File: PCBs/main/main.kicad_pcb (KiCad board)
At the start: 2 copper layers, 91 x 56.5 mm, 6 parts, among them J1 chambers 03-04, J2 chambers 01-02, J3 chambers 05-06, J4 chambers 07-08, J5 chambers 9-10

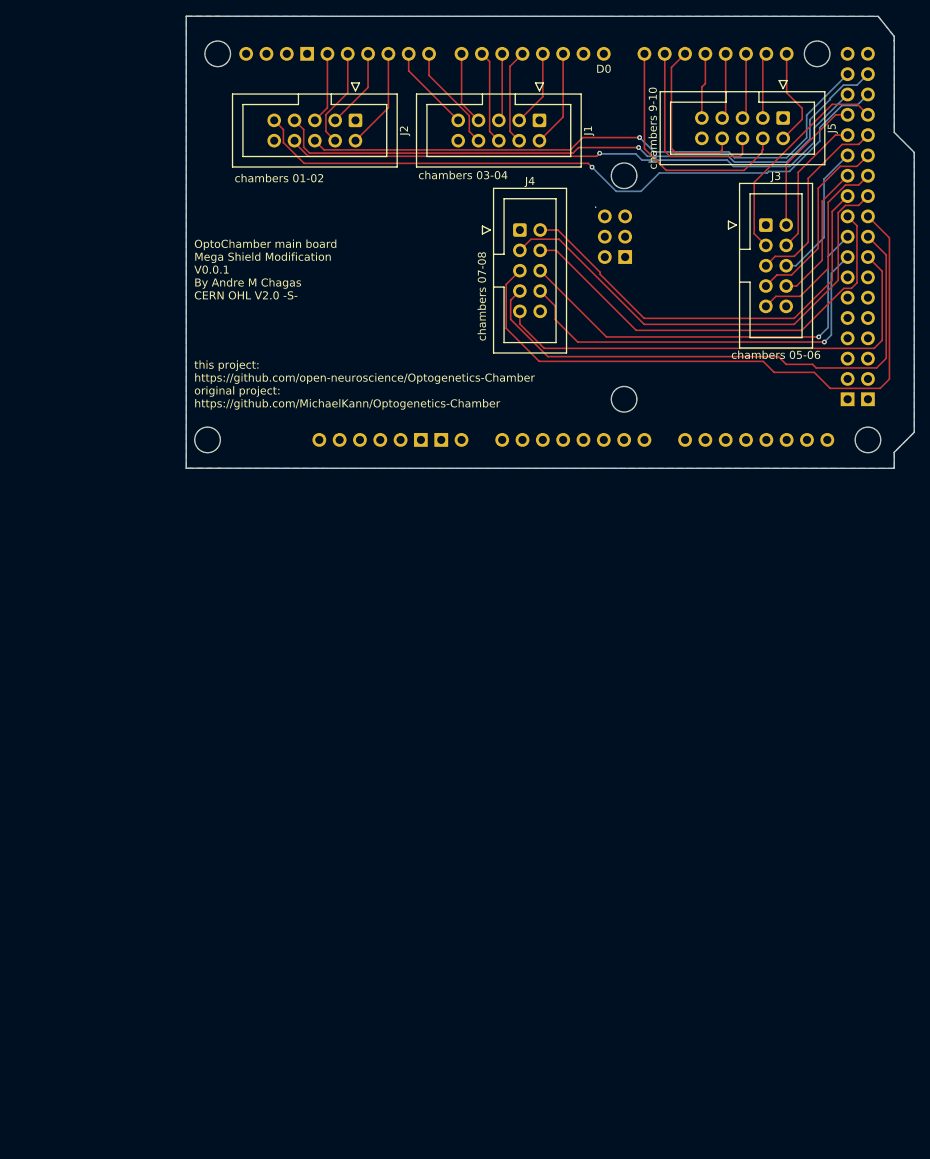
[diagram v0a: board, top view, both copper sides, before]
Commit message: create PCBs for easier replication of the system. It has been altered to use an arduino Mega, instead of an arduino Uno.
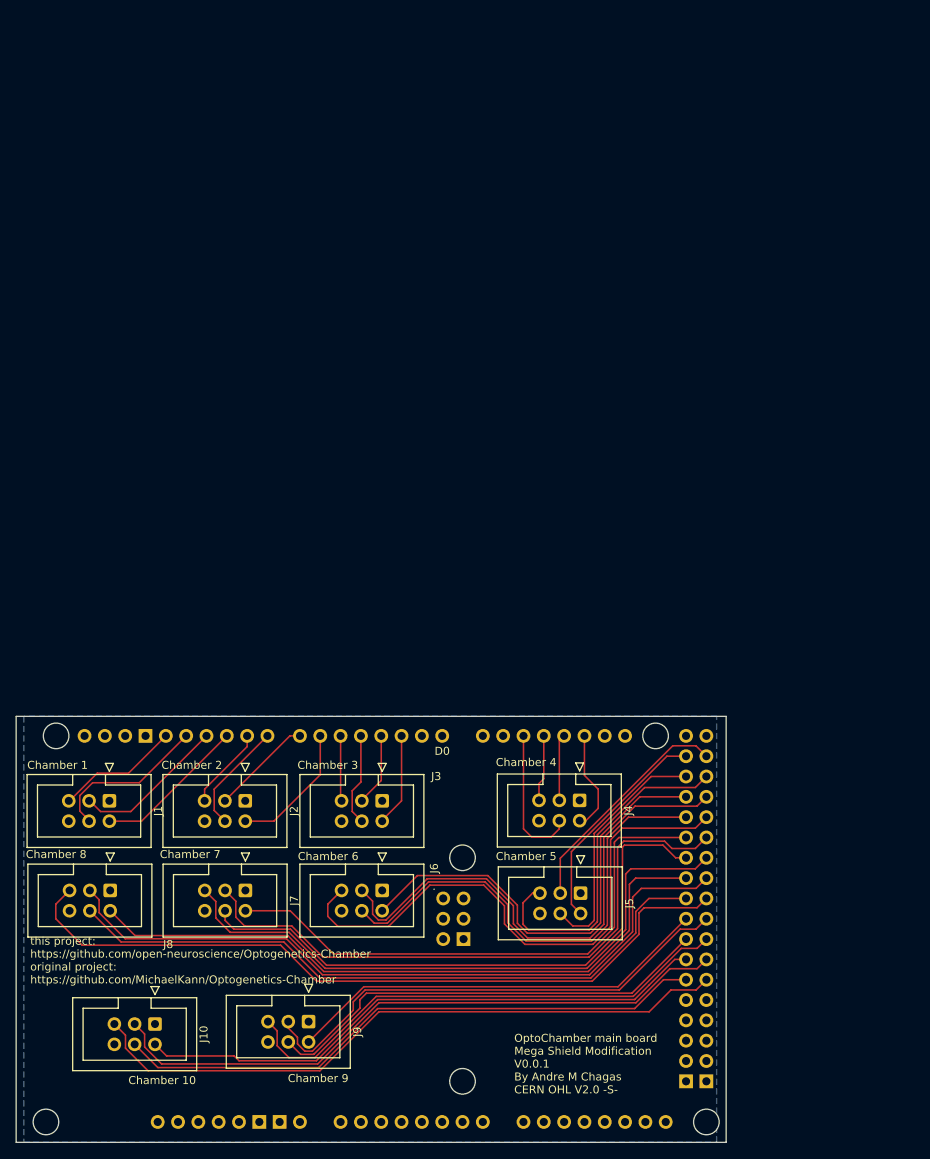
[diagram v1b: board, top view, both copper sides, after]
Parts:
- added J10: Chamber 10, Connector_IDC:IDC-Header_2x03_P2.54mm_Vertical, F.Cu at (94.6, 161.0)
- added J6: Chamber 6, Connector_IDC:IDC-Header_2x03_P2.54mm_Vertical, F.Cu at (123.0, 144.3)
- added J7: Chamber 7, Connector_IDC:IDC-Header_2x03_P2.54mm_Vertical, F.Cu at (105.9, 144.3)
- added J8: Chamber 8, Connector_IDC:IDC-Header_2x03_P2.54mm_Vertical, F.Cu at (89.0, 144.3)
- added J9: Chamber 9, Connector_IDC:IDC-Header_2x03_P2.54mm_Vertical, F.Cu at (113.8, 160.7)
- J1: value chambers 03-04 -> Chamber 1; footprint Connector_IDC:IDC-Header_2x05_P2.54mm_Vertical -> Connector_IDC:IDC-Header_2x03_P2.54mm_Vertical
- J2: value chambers 01-02 -> Chamber 2; footprint Connector_IDC:IDC-Header_2x05_P2.54mm_Vertical -> Connector_IDC:IDC-Header_2x03_P2.54mm_Vertical
- J3: value chambers 05-06 -> Chamber 3; footprint Connector_IDC:IDC-Header_2x05_P2.54mm_Vertical -> Connector_IDC:IDC-Header_2x03_P2.54mm_Vertical
- J4: value chambers 07-08 -> Chamber 4; footprint Connector_IDC:IDC-Header_2x05_P2.54mm_Vertical -> Connector_IDC:IDC-Header_2x03_P2.54mm_Vertical
- J5: value chambers 9-10 -> Chamber 5; footprint Connector_IDC:IDC-Header_2x05_P2.54mm_Vertical -> Connector_IDC:IDC-Header_2x03_P2.54mm_Vertical
- moved J1 100.6 mm to (88.9, 133.1)
- moved J5 100.1 mm to (147.8, 144.6)
- moved A2 87.6 mm to (67.0, 175.7)
- moved J3 86.5 mm to (123.0, 133.1), turned to -90 degrees
- moved J2 86.2 mm to (105.9, 133.1)
- moved J4 71.7 mm to (147.7, 133.0), turned to -90 degrees
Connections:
- A2 pad D10: Net-(J2-Pin_2) -> Net-(J1-Pin_2)
- A2 pad D11: Net-(J2-Pin_3) -> Net-(J1-Pin_3)
- A2 pad D12: Net-(J2-Pin_4) -> Net-(J1-Pin_4)
- A2 pad D13: Net-(J2-Pin_5) -> Net-(J1-Pin_5)
- A2 pad D14: Net-(A2-D14/TX3) -> unconnected-(A2-D14/TX3-PadD14)
- A2 pad D15: Net-(A2-D15/RX3) -> unconnected-(A2-D15/RX3-PadD15)
- A2 pad D20: Net-(A2-D20/SDA) -> unconnected-(A2-D20/SDA-PadD20)
- A2 pad D21: Net-(A2-D21/SCL) -> unconnected-(A2-D21/SCL-PadD21)
- A2 pad D22: Net-(J2-Pin_6) -> Net-(J5-Pin_2)
- A2 pad D23: Net-(J2-Pin_7) -> Net-(J5-Pin_3)
- A2 pad D24: Net-(J2-Pin_8) -> Net-(J5-Pin_4)
- A2 pad D25: Net-(J2-Pin_9) -> Net-(J5-Pin_5)
- A2 pad D26: Net-(J3-Pin_2) -> Net-(J6-Pin_2)
- A2 pad D27: Net-(J3-Pin_3) -> Net-(J6-Pin_3)
- A2 pad D28: Net-(J3-Pin_4) -> Net-(J6-Pin_4)
- A2 pad D29: Net-(J3-Pin_5) -> Net-(J6-Pin_5)
- A2 pad D30: Net-(J3-Pin_6) -> Net-(J7-Pin_2)
- A2 pad D31: Net-(J3-Pin_7) -> Net-(J7-Pin_3)
- A2 pad D32: Net-(J3-Pin_8) -> Net-(J7-Pin_4)
- A2 pad D33: Net-(J3-Pin_9) -> Net-(J7-Pin_5)
- A2 pad D34: Net-(J4-Pin_2) -> Net-(J8-Pin_2)
- A2 pad D35: Net-(J4-Pin_3) -> Net-(J8-Pin_3)
- A2 pad D36: Net-(J4-Pin_4) -> Net-(J8-Pin_4)
- A2 pad D37: Net-(J4-Pin_5) -> Net-(J8-Pin_5)
- A2 pad D38: Net-(J4-Pin_6) -> Net-(J9-Pin_2)
- A2 pad D39: Net-(J4-Pin_7) -> Net-(J9-Pin_3)
- A2 pad D4: Net-(J1-Pin_4) -> Net-(J3-Pin_4)
- A2 pad D40: Net-(J4-Pin_8) -> Net-(J9-Pin_4)
- A2 pad D41: Net-(J4-Pin_9) -> Net-(J9-Pin_5)
- A2 pad D42: unconnected-(A2-PadD42) -> Net-(J10-Pin_2)
- A2 pad D43: unconnected-(A2-PadD43) -> Net-(J10-Pin_3)
- A2 pad D44: unconnected-(A2-PadD44) -> Net-(J10-Pin_4)
- A2 pad D45: unconnected-(A2-PadD45) -> Net-(J10-Pin_5)
- A2 pad D5: Net-(J1-Pin_5) -> Net-(J3-Pin_5)
- A2 pad D6: Net-(J1-Pin_6) -> Net-(J2-Pin_2)
- A2 pad D7: Net-(J1-Pin_7) -> Net-(J2-Pin_3)
- A2 pad D8: Net-(J1-Pin_8) -> Net-(J2-Pin_4)
- A2 pad D9: Net-(J1-Pin_9) -> Net-(J2-Pin_5)
- J1 pad 2: Net-(A2-D2_INT0) -> Net-(J1-Pin_2)
- J1 pad 3: Net-(A2-D3_INT1) -> Net-(J1-Pin_3)
- J1 pad 6: Net-(J1-Pin_6) -> unconnected-(J1-Pin_6-Pad6)
- J2 pad 6: Net-(J2-Pin_6) -> unconnected-(J2-Pin_6-Pad6)
- J3 pad 2: Net-(J3-Pin_2) -> Net-(A2-D2_INT0)
- J3 pad 3: Net-(J3-Pin_3) -> Net-(A2-D3_INT1)
- J3 pad 6: Net-(J3-Pin_6) -> unconnected-(J3-Pin_6-Pad6)
- J4 pad 2: Net-(J4-Pin_2) -> Net-(A2-D19/RX1)
- J4 pad 3: Net-(J4-Pin_3) -> Net-(A2-D18/TX1)
- J4 pad 4: Net-(J4-Pin_4) -> Net-(A2-D16/TX2)
- J4 pad 5: Net-(J4-Pin_5) -> Net-(A2-D17/RX2)
- J4 pad 6: Net-(J4-Pin_6) -> unconnected-(J4-Pin_6-Pad6)
- J5 pad 2: Net-(A2-D21/SCL) -> Net-(J5-Pin_2)
- J5 pad 3: Net-(A2-D20/SDA) -> Net-(J5-Pin_3)
- J5 pad 4: Net-(A2-D14/TX3) -> Net-(J5-Pin_4)
- J5 pad 5: Net-(A2-D19/RX1) -> Net-(J5-Pin_5)
- J5 pad 6: Net-(A2-D15/RX3) -> unconnected-(J5-Pin_6-Pad6)
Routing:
- net Net-(J8-Pin_5): track 0.00 -> 94.7 mm
- net Net-(J8-Pin_3): track 0.00 -> 89.9 mm
- net Net-(J2-Pin_9): track 84.9 -> 0.00 mm, vias 1 -> 0
- net Net-(J8-Pin_4): track 0.00 -> 83.7 mm
- net Net-(J8-Pin_2): track 0.00 -> 83.3 mm
- net Net-(J10-Pin_5): track 0.00 -> 82.1 mm
- net Net-(J2-Pin_7): track 81.8 -> 0.00 mm, vias 1 -> 0
- net Net-(J4-Pin_5): track 80.9 -> 0.00 mm
- net Net-(J10-Pin_3): track 0.00 -> 79.9 mm
- net Net-(J7-Pin_5): track 0.00 -> 77.7 mm
- net Net-(J7-Pin_3): track 0.00 -> 77.7 mm
- net Net-(J2-Pin_8): track 75.7 -> 0.00 mm, vias 1 -> 0
- net Net-(J2-Pin_6): track 74.7 -> 0.00 mm, vias 1 -> 0
- net Net-(J10-Pin_4): track 0.00 -> 74.7 mm
- net Net-(J7-Pin_4): track 0.00 -> 74.0 mm
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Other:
- board size 91 x 56.5 mm -> 88.8 x 53.2 mm
